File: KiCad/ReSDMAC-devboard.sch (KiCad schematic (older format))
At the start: 7 parts, among them J2 USB_B_Micro, J3 Conn_02x01, U1 PLCC-84-Plug, U2 Super_DMAC_SMD_socket, U3 Super_DMAC_TH_socket

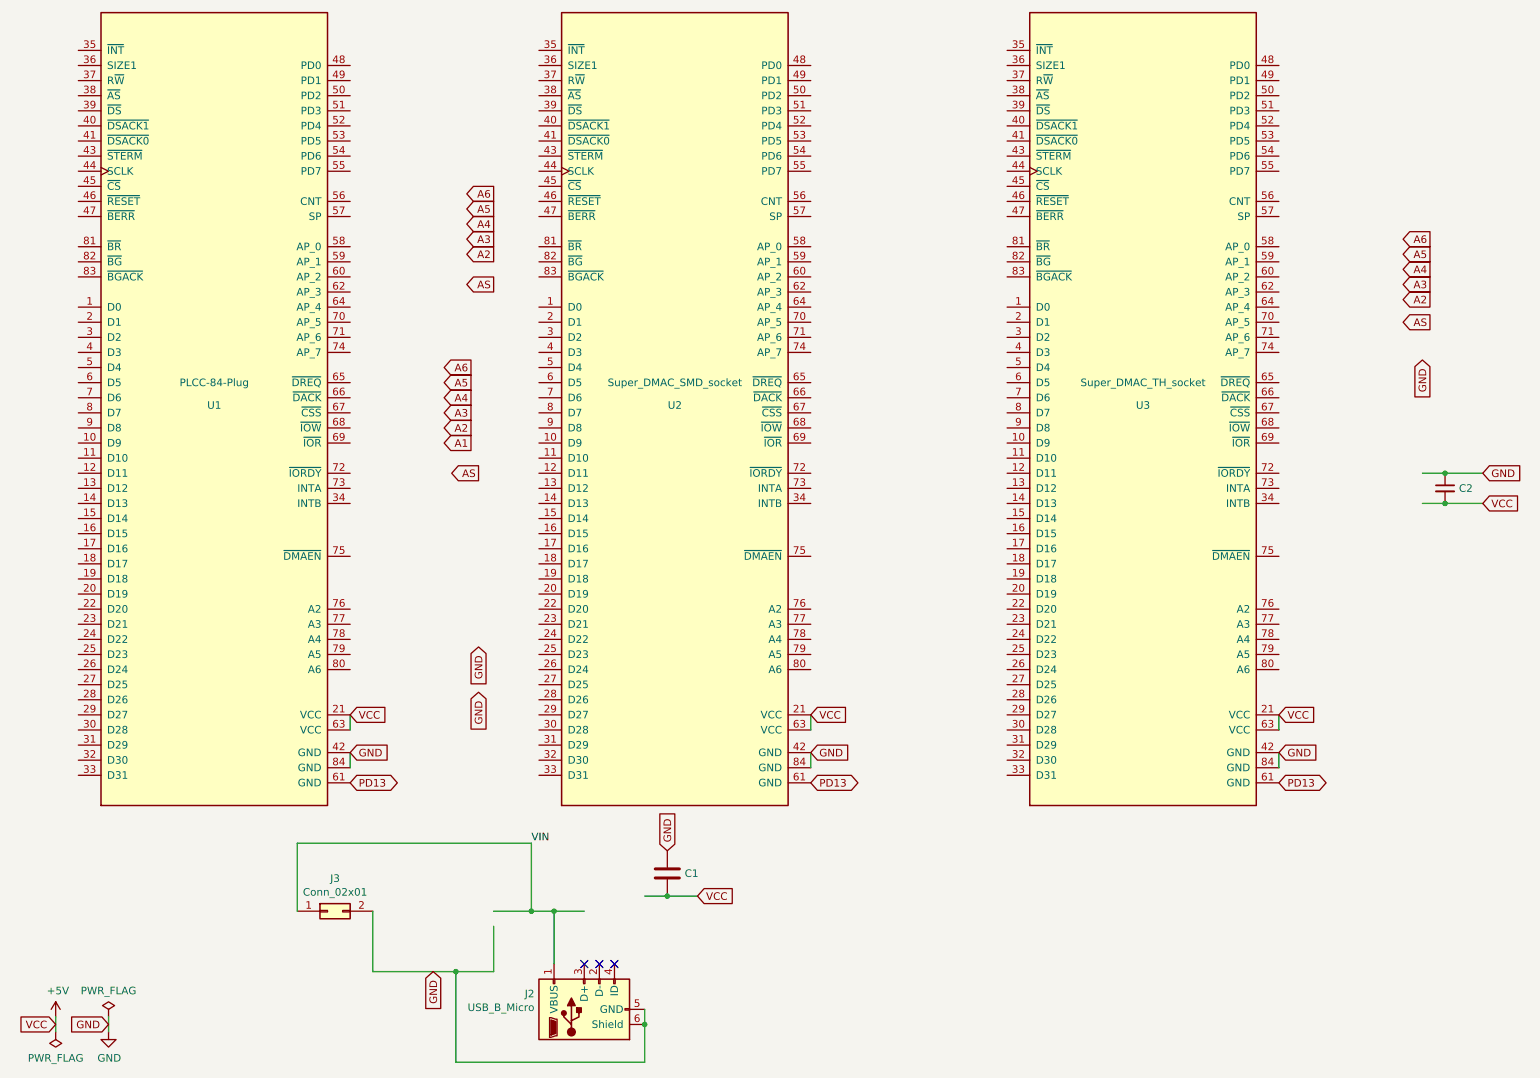
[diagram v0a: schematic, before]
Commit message: Added nets and started routing
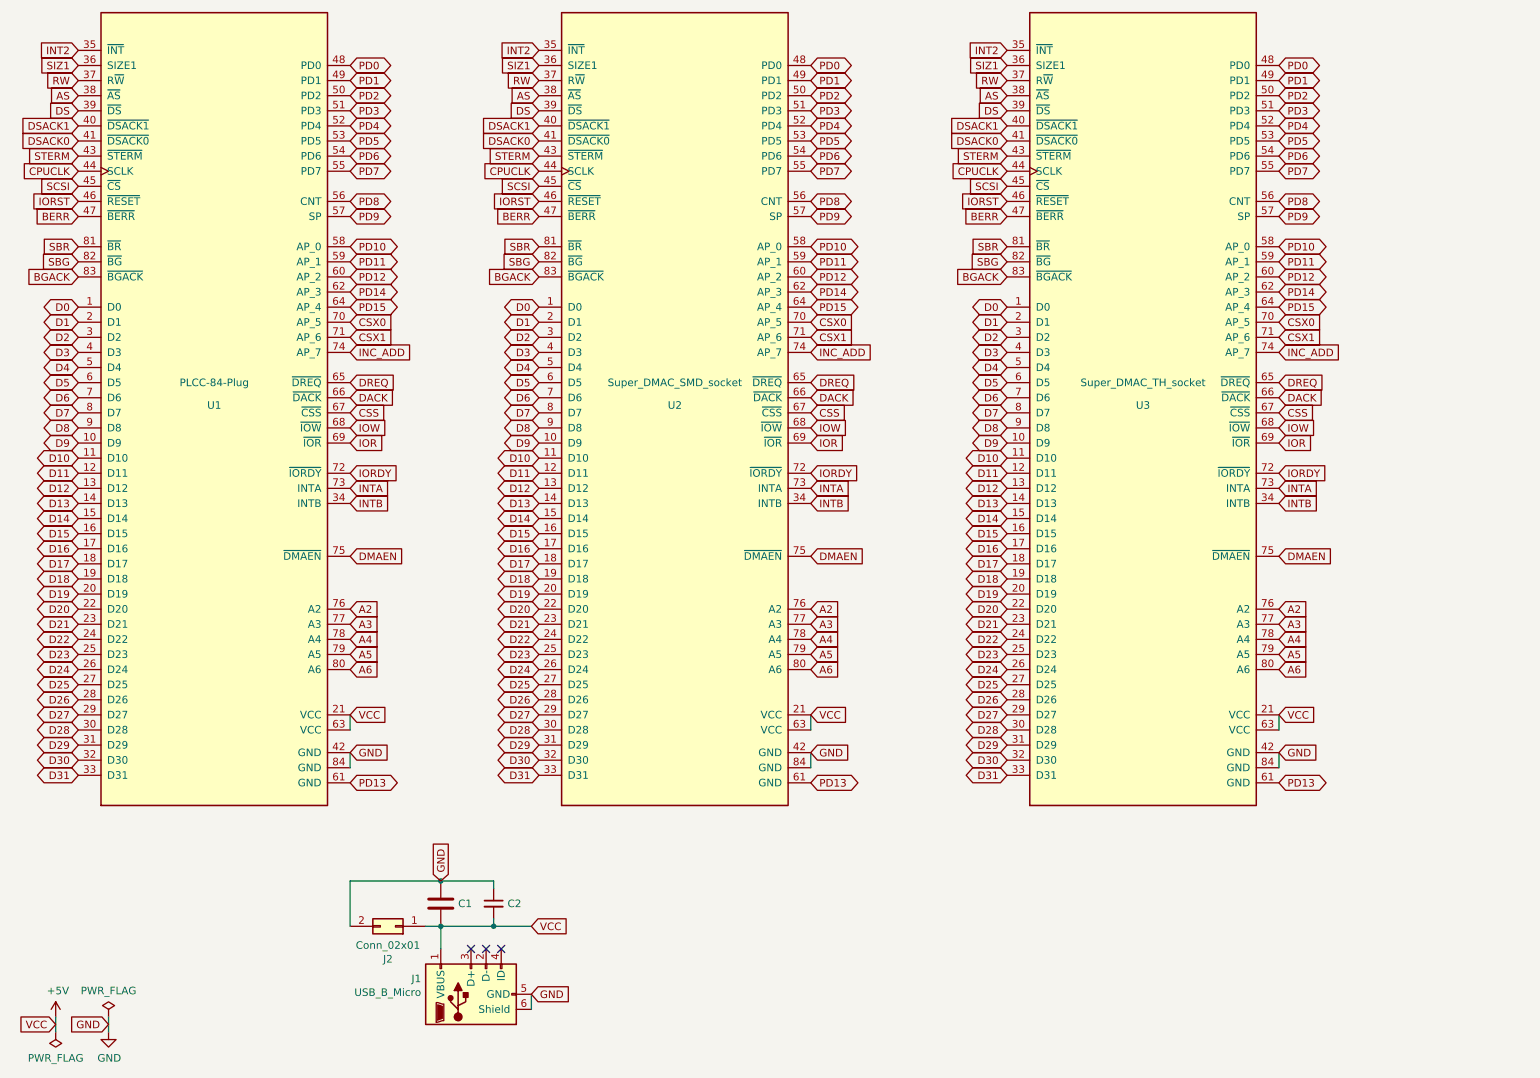
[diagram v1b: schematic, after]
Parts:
- renumbered J2 to J1, J3 to J2
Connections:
- net labels added: BERR, BGACK, CPUCLK, CSS, CSX0, CSX1, D0, D1, D10, D11, D12, D13, D14, D15, D16, D17, D18, D19, D2, D20, D21, D22, D23, D24, D25, D26, D27, D28, D29, D3, D30, D31, D4, D5, D6, D7, D8, D9, DACK, DMAEN, DREQ, DS, DSACK0, DSACK1, INC_ADD, INT2, INTA, INTB, IOR, IORDY, IORST, IOW, PD0, PD1, PD10, PD11, PD12, PD14, PD15, PD2, PD3, PD4, PD5, PD6, PD7, PD8, PD9, RW, SBG, SBR, SCSI, SIZ1, STERM
- net labels removed: A1, VIN
- wire segments 29 -> 18
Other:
- moved on the sheet: C1, C2, J1, J2

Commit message: Fixed caps and power circuit routing
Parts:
- added C?: 0.1uF, Capacitor_SMD:C_0805_2012Metric_Pad1.18x1.45mm_HandSolder, symbol Device:C_Small
- C1: value C -> 100uF Radial Pitch_2.5mm; footprint Capacitor_SMD:C_1210_3225Metric_Pad1.42x2.65mm_HandSolder -> Capacitor_THT:CP_Radial_D5.0mm_P2.50mm; symbol Device:C -> Device:CP_Small
- C2: value C_Small -> 10uF; footprint Capacitor_SMD:C_1206_3216Metric_Pad1.42x1.75mm_HandSolder -> Capacitor_SMD:C_1206_3216Metric_Pad1.33x1.80mm_HandSolder
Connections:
- net +5V: now also C1.1, C?.2; no longer C1.2
- net GND: now also C1.2, C?.1; no longer C1.1
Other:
- moved on the sheet: C2
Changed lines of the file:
@@
 Text GLabel 4000 7200 2    50   Input ~ 0
 GND
-Text GLabel 4000 6750 2    50   Input ~ 0
+Text GLabel 4150 6750 2    50   Input ~ 0
 VCC
 Text GLabel 8950 4650 2    50   Input ~ 0
@@
 A6
 $Comp
-L Device:C C1
+L Device:CP_Small C1
 U 1 1 60DB5D56
 P 3400 6600
-F 0 "C1" H 3515 6600 50  0000 L CNN
-F 1 "C" H 3515 6555 50  0001 L CNN
-F 2 "Capacitor_SMD:C_1210_3225Metric_Pad1.42x2.65mm_HandSolder" H 3438 6450 50  0001 C CNN
+F 0 "C1" H 3500 6600 50  0000 L CNN
+F 1 "100uF Radial Pitch_2.5mm" H 3450 6500 50  0000 L CNN
+F 2 "Capacitor_THT:CP_Radial_D5.0mm_P2.50mm" H 3438 6450 50  0001 C CNN
 F 3 "~" H 3400 6600 50  0001 C CNN
 	1    3400 6600
-	1    0    0    -1
+	-1   0    0    1
 $EndComp
 Text GLabel 3400 6450 1    50   Input ~ 0
@@
 L Device:C_Small C2
 U 1 1 60DBB6F0
-P 3750 6600
-F 0 "C2" H 3842 6600 50  0000 L CNN
-F 1 "C_Small" H 3842 6555 50  0001 L CNN
-F 2 "Capacitor_SMD:C_1206_3216Metric_Pad1.42x1.75mm_HandSolder" H 3750 6600 50  0001 C CNN
-F 3 "~" H 3750 6600 50  0001 C CNN
-	1    3750 6600
+P 3700 6600
+F 0 "C2" H 3750 6550 50  0000 L CNN
+F 1 "10uF" H 3700 6700 50  0000 L CNN
+F 2 "Capacitor_SMD:C_1206_3216Metric_Pad1.33x1.80mm_HandSolder" H 3700 6600 50  0001 C CNN
+F 3 "~" H 3700 6600 50  0001 C CNN
+	1    3700 6600
 	1    0    0    -1
 $EndComp
@@
 Wire Wire Line
 	2800 6450 3400 6450
-Wire Wire Line
-	3400 6450 3750 6450
-Wire Wire Line
-	3750 6450 3750 6500
 Connection ~ 3400 6450
-Wire Wire Line
-	3400 6750 3750 6750
-Wire Wire Line
-	3750 6750 3750 6700
-Wire Wire Line
-	3750 6750 4000 6750
-Connection ~ 3750 6750
 Text GLabel 1000 2650 0    50   BiDi ~ 0
 D0
@@
 Text GLabel 8950 4300 2    50   Input ~ 0
 DMAEN
+Wire Wire Line
+	3400 6500 3400 6450
+Wire Wire Line
+	3400 6750 3400 6700
+$Comp
+L Device:C_Small C?
+U 1 1 6658B651
+P 4000 6600
+F 0 "C?" H 4100 6600 50  0000 L CNN
+F 1 "0.1uF" H 4050 6700 50  0000 L CNN
+F 2 "Capacitor_SMD:C_0805_2012Metric_Pad1.18x1.45mm_HandSolder" H 4000 6600 50  0001 C CNN
+F 3 "~" H 4000 6600 50  0001 C CNN
+	1    4000 6600
+	1    0    0    -1
+$EndComp
+Wire Wire Line
+	3400 6450 3700 6450
+Wire Wire Line
+	3400 6750 3700 6750
+Wire Wire Line
+	3700 6450 3700 6500
+Connection ~ 3700 6450
+Wire Wire Line
+	3700 6700 3700 6750
+Connection ~ 3700 6750
+Wire Wire Line
+	3700 6750 4000 6750
+Wire Wire Line
+	4000 6500 4000 6450
+Wire Wire Line
+	3700 6450 4000 6450
+Wire Wire Line
+	4000 6700 4000 6750
+Wire Wire Line
+	4000 6750 4150 6750
+Connection ~ 4000 6750
 $EndSCHEMATC

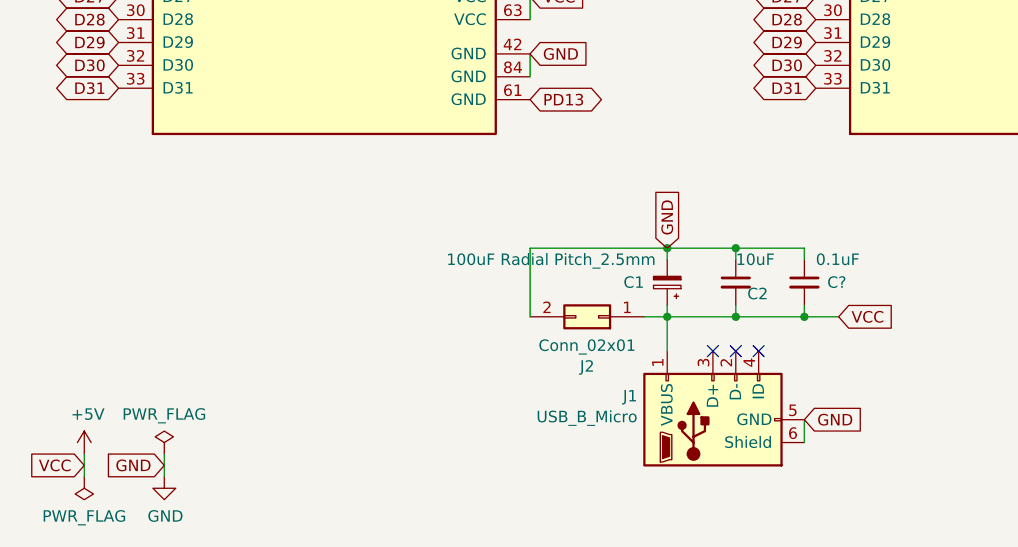
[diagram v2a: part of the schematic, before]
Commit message: Added MountingHole_3.2mm_M3_Pad_Via for grounding wire with ring lug connector
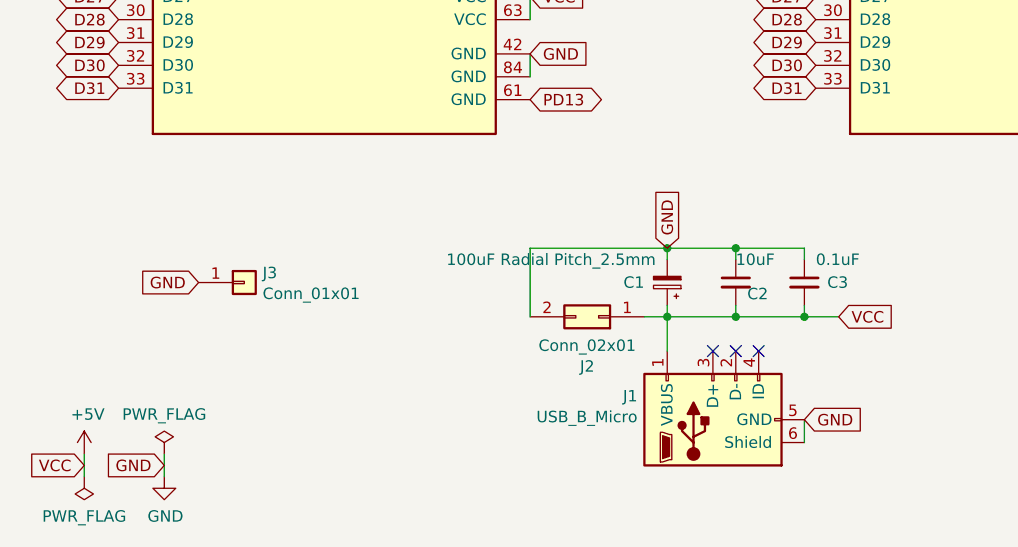
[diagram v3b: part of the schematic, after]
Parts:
- added J3: Conn_01x01, MountingHole:MountingHole_3.2mm_M3_Pad_Via, symbol Connector_Generic:Conn_01x01
- gave numbers to parts that had none: 1
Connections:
- net GND: now also J3.1 (Pin_1)
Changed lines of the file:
@@
 	3400 6750 3400 6700
 $Comp
-L Device:C_Small C?
+L Device:C_Small C3
 U 1 1 6658B651
 P 4000 6600
-F 0 "C?" H 4100 6600 50  0000 L CNN
+F 0 "C3" H 4100 6600 50  0000 L CNN
 F 1 "0.1uF" H 4050 6700 50  0000 L CNN
 F 2 "Capacitor_SMD:C_0805_2012Metric_Pad1.18x1.45mm_HandSolder" H 4000 6600 50  0001 C CNN
@@
 	4000 6750 4150 6750
 Connection ~ 4000 6750
+$Comp
+L Connector_Generic:Conn_01x01 J3
+U 1 1 665B1376
+P 1550 6600
+F 0 "J3" H 1630 6642 50  0000 L CNN
+F 1 "Conn_01x01" H 1630 6551 50  0000 L CNN
+F 2 "MountingHole:MountingHole_3.2mm_M3_Pad_Via" H 1550 6600 50  0001 C CNN
+F 3 "~" H 1550 6600 50  0001 C CNN
+	1    1550 6600
+	1    0    0    -1
+$EndComp
+Text GLabel 1350 6600 0    50   Input ~ 0
+GND
 $EndSCHEMATC
